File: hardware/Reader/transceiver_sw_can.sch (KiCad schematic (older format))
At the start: 12 parts, among them IC6 TH8056KDC-AAA-014-RE

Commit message: Completed Reader schematics for version 0.0.01
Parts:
- removed JP_SWCAN_1: Jumper_NO_Small, symbol Device:Jumper_NO_Small
- added J_SWCAN_1: 282832-2, footprints:282832-2, symbol 2828322:282832-2
- Q_SWCAN_1: footprint footprints:RESC0603X26N -> footprints:SOT95P230X110-3N
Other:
- note added: "High-Speed Load Circuit - Do not connect J_SWCAN_1 for Read-only"
- note removed: "High-Speed Load Circuit - Omit this for Read-only"
- moved on the sheet: C_SWCAN_2, Q_SWCAN_1, R_SWCAN_6, R_SWCAN_7
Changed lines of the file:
@@
 $Descr USLetter 11000 8500
 encoding utf-8
-Sheet 15 17
+Sheet 15 18
 Title "CANnect Reader | Single Wire CAN Transceiver"
 Date "2020-10-20"
-Rev "0.0.1"
+Rev "0.0.01"
 Comp "CANtech"
 Comment1 "Created by Choong Jin Ng | jin8383@gmail.com"
@@
 L power:GND #PWR0183
 U 1 1 5FBCDB6B
-P 3650 4500
-F 0 "#PWR0183" H 3650 4250 50  0001 C CNN
-F 1 "GND" H 3655 4327 50  0000 C CNN
-F 2 "" H 3650 4500 50  0001 C CNN
-F 3 "" H 3650 4500 50  0001 C CNN
-	1    3650 4500
+P 3950 4500
+F 0 "#PWR0183" H 3950 4250 50  0001 C CNN
+F 1 "GND" H 3955 4327 50  0000 C CNN
+F 2 "" H 3950 4500 50  0001 C CNN
+F 3 "" H 3950 4500 50  0001 C CNN
+	1    3950 4500
 	1    0    0    -1
 $EndComp
@@
 L Device:R_Small R_SWCAN_6
 U 1 1 5FBCE6CE
-P 2650 4100
-F 0 "R_SWCAN_6" H 2709 4146 50  0000 L CNN
-F 1 "130" H 2709 4055 50  0000 L CNN
-F 2 "footprints:RESC0603X26N" H 2650 4100 50  0001 C CNN
-F 3 "https://www.yageo.com/upload/media/product/productsearch/datasheet/rchip/PYu-RC_Group_51_RoHS_L_11.pdf" H 2650 4100 50  0001 C CNN
-F 4 "RC0201FR-07130RL" H 2650 4100 50  0001 C CNN "Part Name"
-	1    2650 4100
-	1    0    0    -1
-$EndComp
-Text HLabel 1550 4700 0    50   BiDi ~ 0
+P 2600 4550
+F 0 "R_SWCAN_6" H 2659 4596 50  0000 L CNN
+F 1 "130" H 2659 4505 50  0000 L CNN
+F 2 "footprints:RESC0603X26N" H 2600 4550 50  0001 C CNN
+F 3 "https://www.yageo.com/upload/media/product/productsearch/datasheet/rchip/PYu-RC_Group_51_RoHS_L_11.pdf" H 2600 4550 50  0001 C CNN
+F 4 "RC0201FR-07130RL" H 2600 4550 50  0001 C CNN "Part Name"
+	1    2600 4550
+	1    0    0    -1
+$EndComp
+Text HLabel 1500 5150 0    50   BiDi ~ 0
 SW_CAN_LOAD
 $Comp
 L NX7002AK_215:NX7002AK,215 Q_SWCAN_1
 U 1 1 5FBCED49
-P 2550 4600
-F 0 "Q_SWCAN_1" H 2748 4596 50  0000 L CNN
-F 1 "NX7002AK,215" H 2748 4505 50  0000 L CNN
-F 2 "footprints:RESC0603X26N" H 2550 4600 50  0001 L BNN
-F 3 "1.1mm" H 2550 4600 50  0001 L BNN
-F 4 "Nexperia" H 2550 4600 50  0001 L BNN "Field4"
-F 5 "7" H 2550 4600 50  0001 L BNN "Field5"
-F 6 "IPC-7351B" H 2550 4600 50  0001 L BNN "Field6"
-	1    2550 4600
+P 2500 5050
+F 0 "Q_SWCAN_1" H 2698 5046 50  0000 L CNN
+F 1 "NX7002AK,215" H 2698 4955 50  0000 L CNN
+F 2 "footprints:SOT95P230X110-3N" H 2500 5050 50  0001 L BNN
+F 3 "https://assets.nexperia.com/documents/data-sheet/NX7002AK.pdf" H 2500 5050 50  0001 L BNN
+F 4 "Nexperia" H 2500 5050 50  0001 L BNN "Field4"
+F 5 "7" H 2500 5050 50  0001 L BNN "Field5"
+F 6 "IPC-7351B" H 2500 5050 50  0001 L BNN "Field6"
+	1    2500 5050
 	1    0    0    -1
 $EndComp
@@
 L Device:R_Small R_SWCAN_7
 U 1 1 5FBCFFA6
-P 2000 4950
-F 0 "R_SWCAN_7" H 2059 4996 50  0000 L CNN
-F 1 "10k" H 2059 4905 50  0000 L CNN
-F 2 "footprints:RESC1608X55N" H 2000 4950 50  0001 C CNN
-F 3 "https://www.yageo.com/upload/media/product/productsearch/datasheet/rchip/PYu-RT_1-to-0.01_RoHS_L_12.pdf" H 2000 4950 50  0001 C CNN
-F 4 "RT0603FRE0710KL" H 2000 4950 50  0001 C CNN "Part Name"
-	1    2000 4950
-	1    0    0    -1
-$EndComp
-Wire Wire Line
-	1550 4700 2000 4700
-Wire Wire Line
-	2000 4850 2000 4700
-Connection ~ 2000 4700
-Wire Wire Line
-	2000 4700 2350 4700
-Wire Wire Line
-	2650 4400 2650 4200
-Wire Wire Line
-	2050 2650 2650 2650
-$Comp
-L Device:Jumper_NO_Small JP_SWCAN_1
-U 1 1 5FBD0A1B
-P 2650 3400
-F 0 "JP_SWCAN_1" V 2604 3448 50  0000 L CNN
-F 1 "Jumper_NO_Small" V 2695 3448 50  0000 L CNN
-F 2 "" H 2650 3400 50  0001 C CNN
-F 3 "~" H 2650 3400 50  0001 C CNN
-	1    2650 3400
-	0    1    1    0
-$EndComp
-Wire Wire Line
-	2650 3300 2650 2650
-Connection ~ 2650 2650
-Wire Wire Line
-	2650 2650 2850 2650
-Wire Wire Line
-	2650 3500 2650 4000
+P 1950 5400
+F 0 "R_SWCAN_7" H 2009 5446 50  0000 L CNN
+F 1 "10k" H 2009 5355 50  0000 L CNN
+F 2 "footprints:RESC1608X55N" H 1950 5400 50  0001 C CNN
+F 3 "https://www.yageo.com/upload/media/product/productsearch/datasheet/rchip/PYu-RT_1-to-0.01_RoHS_L_12.pdf" H 1950 5400 50  0001 C CNN
+F 4 "RT0603FRE0710KL" H 1950 5400 50  0001 C CNN "Part Name"
+	1    1950 5400
+	1    0    0    -1
+$EndComp
+Wire Wire Line
+	1500 5150 1950 5150
+Wire Wire Line
+	1950 5300 1950 5150
+Connection ~ 1950 5150
+Wire Wire Line
+	1950 5150 2300 5150
+Wire Wire Line
+	2600 4850 2600 4650
 $Comp
 L power:GND #PWR0184
 U 1 1 5FBD183F
-P 2650 5200
-F 0 "#PWR0184" H 2650 4950 50  0001 C CNN
-F 1 "GND" H 2655 5027 50  0000 C CNN
-F 2 "" H 2650 5200 50  0001 C CNN
-F 3 "" H 2650 5200 50  0001 C CNN
-	1    2650 5200
-	1    0    0    -1
-$EndComp
-Wire Notes Line
-	2450 3150 3400 3150
-Wire Notes Line
-	3400 3150 3400 5600
-Wire Notes Line
-	3400 5600 950  5600
-Wire Notes Line
-	950  5600 950  4200
-Wire Notes Line
-	950  4200 2450 4200
-Wire Notes Line
-	2450 4200 2450 3150
-Text Notes 3050 5550 2    50   ~ 0
-High-Speed Load Circuit - Omit this for Read-only
-Wire Wire Line
-	2650 4900 2650 5100
-Wire Wire Line
-	2000 5050 2000 5100
-Wire Wire Line
-	2000 5100 2650 5100
-Connection ~ 2650 5100
-Wire Wire Line
-	2650 5100 2650 5200
+P 2600 5650
+F 0 "#PWR0184" H 2600 5400 50  0001 C CNN
+F 1 "GND" H 2605 5477 50  0000 C CNN
+F 2 "" H 2600 5650 50  0001 C CNN
+F 3 "" H 2600 5650 50  0001 C CNN
+	1    2600 5650
+	1    0    0    -1
+$EndComp
+Wire Notes Line
+	900  6050 900  4650
+Wire Notes Line
+	900  4650 2400 4650
+Wire Notes Line
+	2400 4650 2400 3600
+Text Notes 3700 6000 2    50   ~ 0
+High-Speed Load Circuit - Do not connect J_SWCAN_1 for Read-only
+Wire Wire Line
+	2600 5350 2600 5550
+Wire Wire Line
+	1950 5500 1950 5550
+Wire Wire Line
+	1950 5550 2600 5550
+Connection ~ 2600 5550
+Wire Wire Line
+	2600 5550 2600 5650
 $Comp
 L Device:R_Small R_SWCAN_1
@@
 L Device:C C_SWCAN_2
 U 1 1 5FBD6B6E
-P 4000 3900
-F 0 "C_SWCAN_2" V 3748 3900 50  0000 C CNN
-F 1 "4.7uF 25V" V 3839 3900 50  0000 C CNN
-F 2 "footprints:C1206C475K3RACAUTO" H 4038 3750 50  0001 C CNN
-F 3 "https://api.kemet.com/component-edge/download/specsheet/C1206C475K3RACAUTO.pdf" H 4000 3900 50  0001 C CNN
-F 4 "C1206C475K3RACAUTO" H 4000 3900 50  0001 C CNN "Part Name"
-	1    4000 3900
+P 4300 3900
+F 0 "C_SWCAN_2" V 4048 3900 50  0000 C CNN
+F 1 "4.7uF 25V" V 4139 3900 50  0000 C CNN
+F 2 "footprints:C1206C475K3RACAUTO" H 4338 3750 50  0001 C CNN
+F 3 "https://api.kemet.com/component-edge/download/specsheet/C1206C475K3RACAUTO.pdf" H 4300 3900 50  0001 C CNN
+F 4 "C1206C475K3RACAUTO" H 4300 3900 50  0001 C CNN "Part Name"
+	1    4300 3900
 	0    1    1    0
 $EndComp
 Wire Wire Line
-	4150 3900 4250 3900
-Wire Wire Line
-	4250 3900 4250 2850
+	4450 3900 4550 3900
+Wire Wire Line
+	4550 3900 4550 2850
 $Comp
 L power:+12V #PWR0187
 U 1 1 5FBD853C
-P 4500 3500
-F 0 "#PWR0187" H 4500 3350 50  0001 C CNN
-F 1 "+12V" H 4515 3673 50  0000 C CNN
-F 2 "" H 4500 3500 50  0001 C CNN
-F 3 "" H 4500 3500 50  0001 C CNN
-	1    4500 3500
-	1    0    0    -1
-$EndComp
-Wire Wire Line
-	4250 3900 4500 3900
-Wire Wire Line
-	4500 3900 4500 3500
-Connection ~ 4250 3900
-Wire Wire Line
-	4250 2850 4750 2850
-Wire Wire Line
-	3650 3050 4750 3050
-Wire Wire Line
-	3650 3050 3650 3900
-Wire Wire Line
-	3650 3900 3850 3900
-Connection ~ 3650 3900
-Wire Wire Line
-	3650 3900 3650 4500
+P 4800 3500
+F 0 "#PWR0187" H 4800 3350 50  0001 C CNN
+F 1 "+12V" H 4815 3673 50  0000 C CNN
+F 2 "" H 4800 3500 50  0001 C CNN
+F 3 "" H 4800 3500 50  0001 C CNN
+	1    4800 3500
+	1    0    0    -1
+$EndComp
+Wire Wire Line
+	4550 3900 4800 3900
+Wire Wire Line
+	4800 3900 4800 3500
+Connection ~ 4550 3900
+Wire Wire Line
+	3950 3050 3950 3900
+Wire Wire Line
+	3950 3900 4150 3900
+Connection ~ 3950 3900
+Wire Wire Line
+	3950 3900 3950 4500
 $Comp
 L power:GND #PWR0188
@@
 Wire Wire Line
 	8150 3600 8750 3600
+$Comp
+L 2828322:282832-2 J_SWCAN_1
+U 1 1 5F9F941C
+P 2600 3750
+F 0 "J_SWCAN_1" H 3128 3806 60  0000 L CNN
+F 1 "282832-2" H 3128 3700 60  0000 L CNN
+F 2 "footprints:282832-2" H 3000 3690 60  0001 C CNN
+F 3 "https://www.te.com/commerce/DocumentDelivery/DDEController?Action=srchrtrv&DocNm=282832&DocType=Customer+Drawing&DocLang=English" H 3128 3594 60  0000 L CNN
+F 4 "282832-2" H 2600 3750 50  0001 C CNN "Part Name"
+	1    2600 3750
+	1    0    0    -1
+$EndComp
+Wire Wire Line
+	2600 3750 2600 2650
+Wire Wire Line
+	2050 2650 2600 2650
+Connection ~ 2600 2650
+Wire Wire Line
+	2600 2650 2850 2650
+Wire Wire Line
+	2600 3850 2600 4450
+Wire Wire Line
+	3950 3050 4750 3050
+Wire Wire Line
+	4550 2850 4750 2850
+Wire Notes Line
+	2400 3600 3650 3600
+Wire Notes Line
+	3650 3600 3650 6050
+Wire Notes Line
+	900  6050 3650 6050
 $EndSCHEMATC

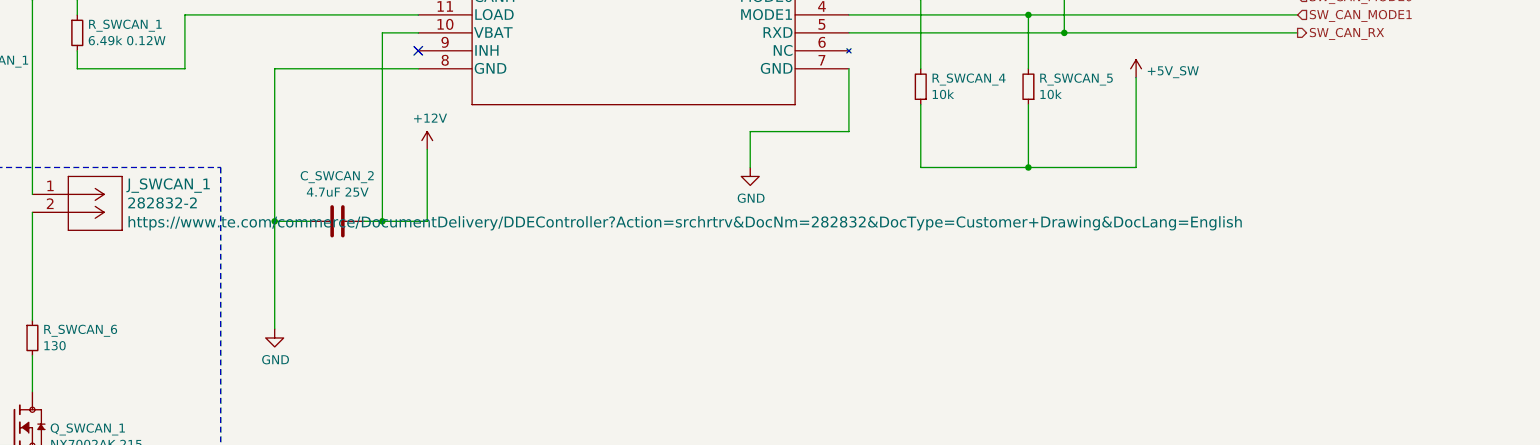
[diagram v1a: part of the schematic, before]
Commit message: Minor changes to schematic design for clarity. Added important IC datasheets. Exported schematics and rough gerber files
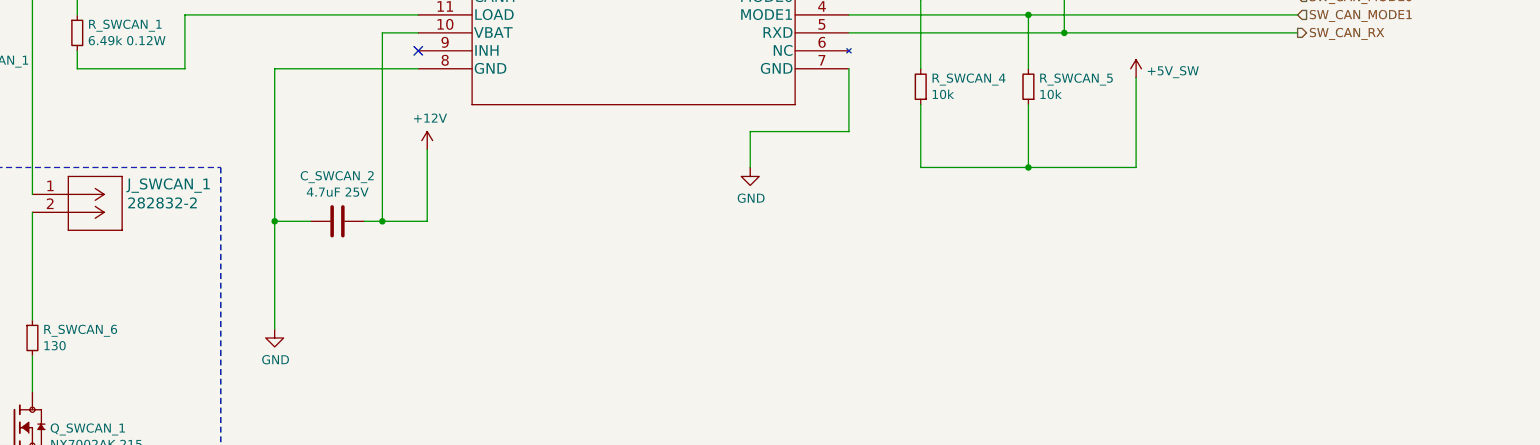
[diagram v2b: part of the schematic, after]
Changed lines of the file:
@@
 $Descr USLetter 11000 8500
 encoding utf-8
-Sheet 15 18
+Sheet 14 18
 Title "CANnect Reader | Single Wire CAN Transceiver"
 Date "2020-10-20"
@@
 F 1 "282832-2" H 3128 3700 60  0000 L CNN
 F 2 "footprints:282832-2" H 3000 3690 60  0001 C CNN
-F 3 "https://www.te.com/commerce/DocumentDelivery/DDEController?Action=srchrtrv&DocNm=282832&DocType=Customer+Drawing&DocLang=English" H 3128 3594 60  0000 L CNN
+F 3 "https://www.te.com/commerce/DocumentDelivery/DDEController?Action=srchrtrv&DocNm=282832&DocType=Customer+Drawing&DocLang=English" H 3128 3594 60  0001 L CNN
 F 4 "282832-2" H 2600 3750 50  0001 C CNN "Part Name"
 	1    2600 3750

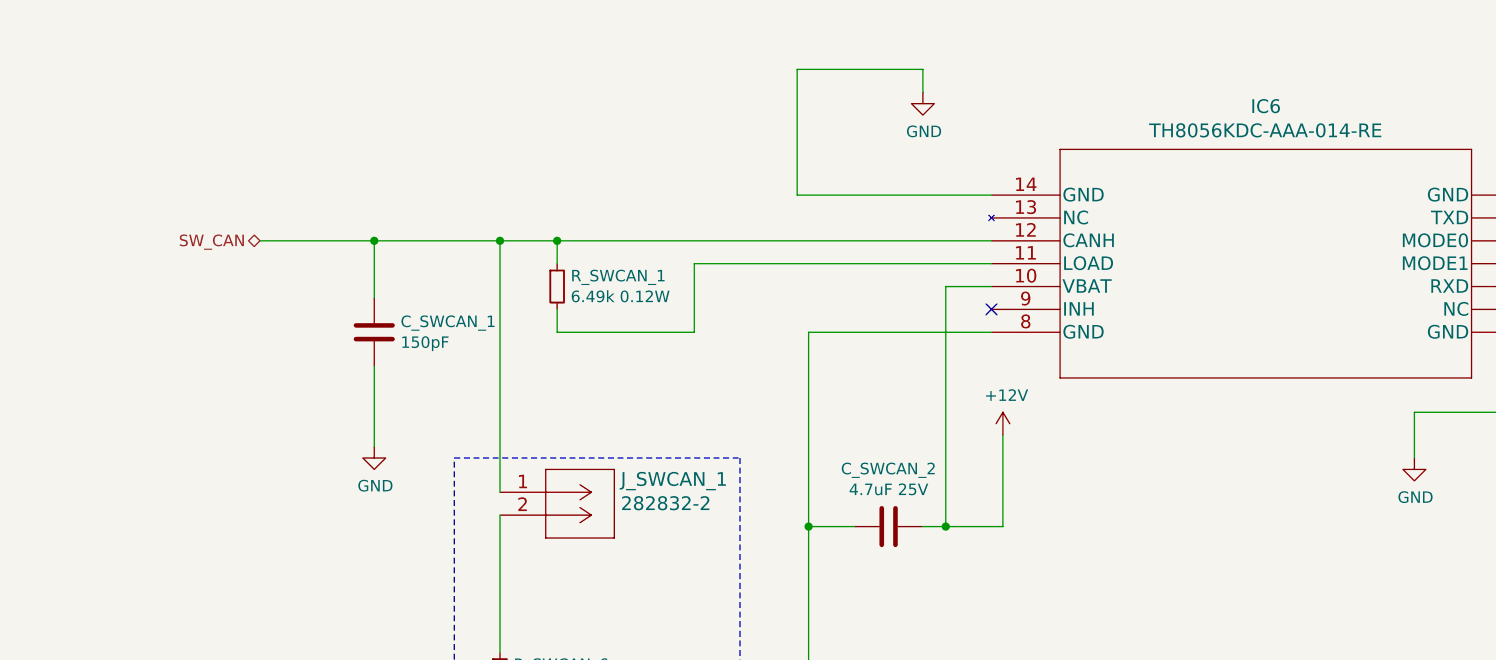
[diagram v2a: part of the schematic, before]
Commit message: Added ESD Protection. Fixed minor bugs on schematic. Attempted placement of components
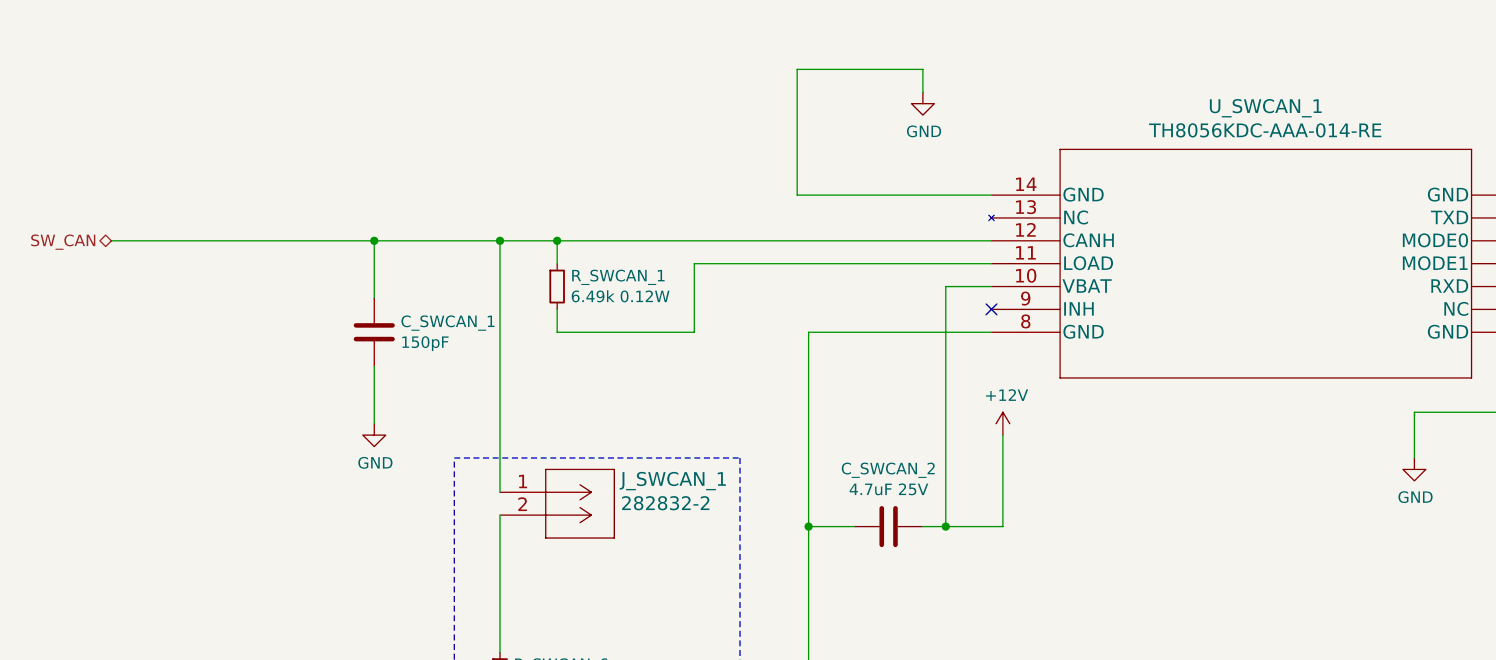
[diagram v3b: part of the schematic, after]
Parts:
- renumbered IC6 to U_SWCAN_1
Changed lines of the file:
@@
 $Descr USLetter 11000 8500
 encoding utf-8
-Sheet 14 18
+Sheet 9 19
 Title "CANnect Reader | Single Wire CAN Transceiver"
-Date "2020-10-20"
-Rev "0.0.01"
+Date "2020-10-25"
+Rev "0.0.03"
 Comp "CANtech"
 Comment1 "Created by Choong Jin Ng | jin8383@gmail.com"
@@
 Comment4 "Component Identifier: SWCAN"
 $EndDescr
-Text HLabel 1550 2650 0    50   BiDi ~ 0
+Text HLabel 900  2650 0    50   BiDi ~ 0
 SW_CAN
 Text HLabel 9650 2550 2    50   Input ~ 0
@@
 SW_CAN_MODE1
 $Comp
-L TH8056KDCAAA014RE:TH8056KDC-AAA-014-RE IC6
+L TH8056KDCAAA014RE:TH8056KDC-AAA-014-RE U_SWCAN_1
 U 1 1 5FBCC1E0
 P 7150 2450
-F 0 "IC6" H 8350 2837 60  0000 C CNN
+F 0 "U_SWCAN_1" H 8350 2837 60  0000 C CNN
 F 1 "TH8056KDC-AAA-014-RE" H 8350 2731 60  0000 C CNN
 F 2 "footprints:TH8056KDC-AAA-014-RE" H 8350 2690 60  0001 C CNN
@@
 $EndComp
 $Comp
-L Device:C C_SWCAN_1
-U 1 1 5FBCCFA6
-P 2050 3050
-F 0 "C_SWCAN_1" H 2165 3096 50  0000 L CNN
-F 1 "150pF" H 2165 3005 50  0000 L CNN
-F 2 "footprints:CAPC1005X55N" H 2088 2900 50  0001 C CNN
-F 3 "https://www.yageo.com/upload/media/product/productsearch/datasheet/mlcc/UPY-GP_NP0_16V-to-50V_18.pdf" H 2050 3050 50  0001 C CNN
-	1    2050 3050
-	1    0    0    -1
-$EndComp
-Wire Wire Line
-	1550 2650 2050 2650
-Wire Wire Line
-	2050 2650 2050 2900
-Connection ~ 2050 2650
-$Comp
 L power:GND #PWR0182
 U 1 1 5FBCD97D
-P 2050 3550
-F 0 "#PWR0182" H 2050 3300 50  0001 C CNN
-F 1 "GND" H 2055 3377 50  0000 C CNN
-F 2 "" H 2050 3550 50  0001 C CNN
-F 3 "" H 2050 3550 50  0001 C CNN
-	1    2050 3550
+P 2050 3450
+F 0 "#PWR0182" H 2050 3200 50  0001 C CNN
+F 1 "GND" H 2055 3277 50  0000 C CNN
+F 2 "" H 2050 3450 50  0001 C CNN
+F 3 "" H 2050 3450 50  0001 C CNN
+	1    2050 3450
 	1    0    0    -1
 $EndComp
@@
 	1    0    0    -1
 $EndComp
-Wire Wire Line
-	2050 3200 2050 3550
 $Comp
 L Device:R_Small R_SWCAN_6
@@
 Wire Wire Line
 	2600 3750 2600 2650
+Connection ~ 2600 2650
+Wire Wire Line
+	2600 2650 2850 2650
+Wire Wire Line
+	2600 3850 2600 4450
+Wire Wire Line
+	3950 3050 4750 3050
+Wire Wire Line
+	4550 2850 4750 2850
+Wire Notes Line
+	2400 3600 3650 3600
+Wire Notes Line
+	3650 3600 3650 6050
+Wire Notes Line
+	900  6050 3650 6050
+Connection ~ 2050 2650
 Wire Wire Line
 	2050 2650 2600 2650
-Connection ~ 2600 2650
-Wire Wire Line
-	2600 2650 2850 2650
-Wire Wire Line
-	2600 3850 2600 4450
-Wire Wire Line
-	3950 3050 4750 3050
-Wire Wire Line
-	4550 2850 4750 2850
-Wire Notes Line
-	2400 3600 3650 3600
-Wire Notes Line
-	3650 3600 3650 6050
-Wire Notes Line
-	900  6050 3650 6050
+Wire Wire Line
+	2050 3200 2050 3450
+Wire Wire Line
+	2050 2650 2050 2900
+$Comp
+L Device:C C_SWCAN_1
+U 1 1 5FBCCFA6
+P 2050 3050
+F 0 "C_SWCAN_1" H 2165 3096 50  0000 L CNN
+F 1 "150pF" H 2165 3005 50  0000 L CNN
+F 2 "footprints:CAPC1005X55N" H 2088 2900 50  0001 C CNN
+F 3 "https://www.yageo.com/upload/media/product/productsearch/datasheet/mlcc/UPY-GP_NP0_16V-to-50V_18.pdf" H 2050 3050 50  0001 C CNN
+	1    2050 3050
+	1    0    0    -1
+$EndComp
+Wire Wire Line
+	900  2650 2050 2650
 $EndSCHEMATC
